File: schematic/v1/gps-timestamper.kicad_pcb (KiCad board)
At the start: 2 copper layers, 80 x 40 mm, 77 parts, among them J1 GPS, J2 Input, J3 PPS_OUT, J4 USB_OTG, J5 SWD, U1 MCP633, U2 MCP633, U3 APU1206K-33, U4 MCP633, U5 MCP633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

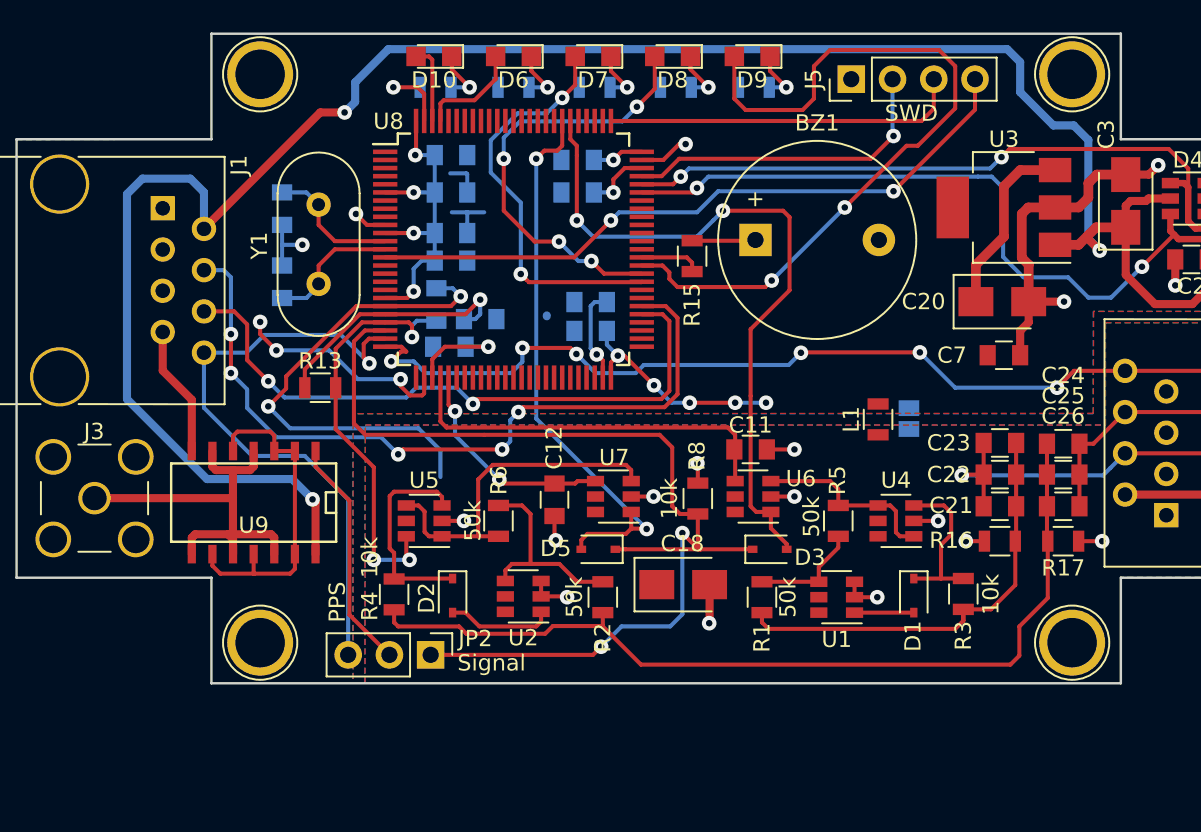
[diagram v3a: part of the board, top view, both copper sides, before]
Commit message: Fix for PCBs: op amps
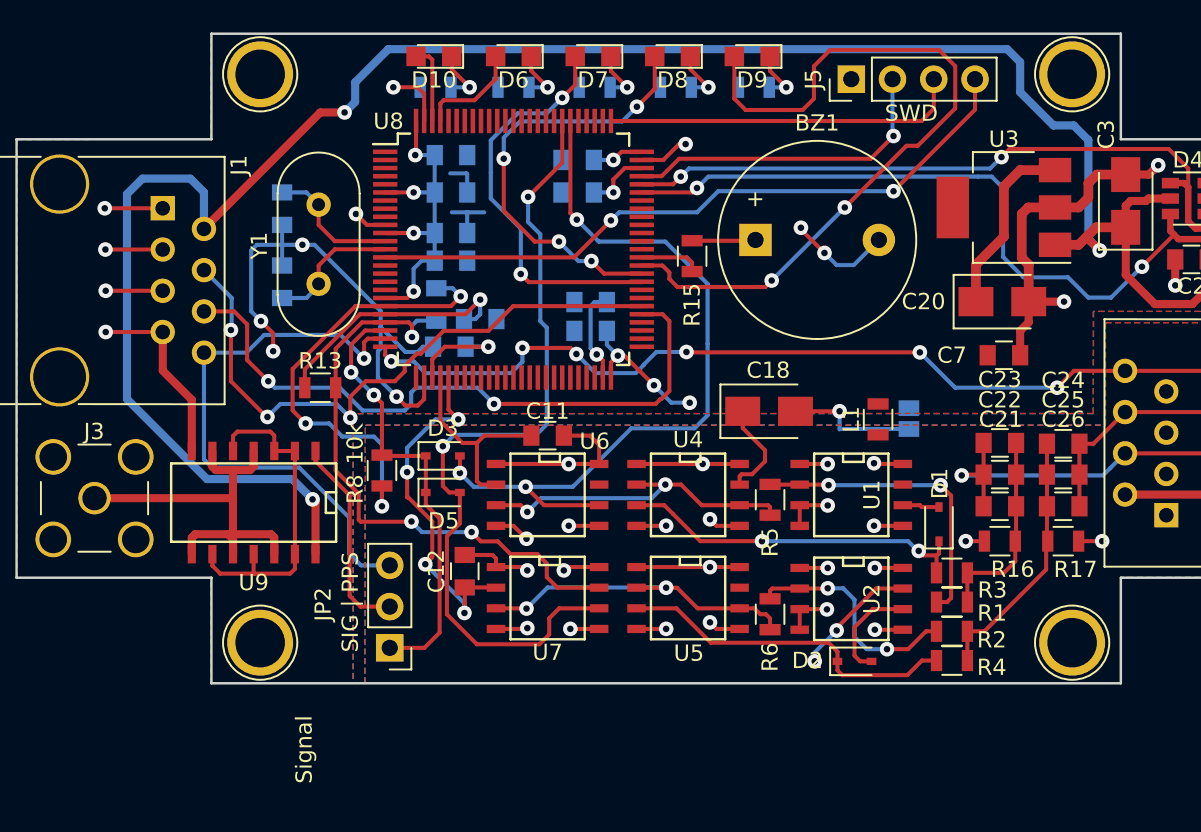
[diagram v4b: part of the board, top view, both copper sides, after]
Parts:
- U1, U2, U4, U5, U6, U7: footprint TO_SOT_Packages_SMD:SOT-23-6 -> SMD_Packages:SOIC-8-N
- U3: value APU1206K-33 -> MCP1826S
- moved R4 34.6 mm to (80.6, 61.6), turned to 0 degrees
- moved D2 25.1 mm to (74.6, 61.6), turned to 0 degrees
- moved R2 21.6 mm to (80.6, 59.8), turned to 0 degrees
- moved D3 20.9 mm to (49.2, 49.0)
- moved U2 20.2 mm to (74.4, 57.8), turned to 270 degrees
- moved R8 19.5 mm to (45.5, 49.9), turned to 90 degrees
- moved R6 17.7 mm to (69.4, 58.8)
- moved U5 16.9 mm to (64.3, 57.8), turned to 270 degrees
- moved U4 12.9 mm to (64.3, 51.4), turned to 270 degrees
- moved U6 12.7 mm to (55.7, 51.4), turned to 270 degrees
- moved C11 12.5 mm to (55.7, 47.8)
- moved C18 11.9 mm to (69.3, 46.2)
- moved R1 11.7 mm to (80.6, 58.0), turned to 0 degrees
- moved D5 10.2 mm to (49.2, 51.2), turned to 0 degrees
- moved U7 7.45 mm to (55.7, 57.8), turned to 270 degrees
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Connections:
- U1 pad 1: Net-(D1-Pad2) -> GNDA
- U1 pad 2: GNDA -> Net-(R1-Pad1)
- U1 pad 4: Net-(R1-Pad1) -> GNDA
- U1 pad 5: Net-(U1-Pad5) -> GNDA
- U1 pad 6: +3.3VA -> Net-(D1-Pad2)
- U2 pad 1: Net-(D2-Pad2) -> GNDA
- U2 pad 2: GNDA -> Net-(R2-Pad1)
- U2 pad 4: Net-(R2-Pad1) -> GNDA
- U2 pad 5: Net-(U2-Pad5) -> GNDA
- U2 pad 6: +3.3VA -> Net-(D2-Pad2)
- U4 pad 1: Net-(R5-Pad1) -> GNDA
- U4 pad 2: GNDA -> Net-(R5-Pad1)
- U4 pad 4: Net-(R5-Pad1) -> GNDA
- U4 pad 5: Net-(U4-Pad5) -> GNDA
- U4 pad 6: +3.3VA -> Net-(R5-Pad1)
- U5 pad 1: Net-(R6-Pad1) -> GNDA
- U5 pad 2: GNDA -> Net-(R6-Pad1)
- U5 pad 4: Net-(R6-Pad1) -> GNDA
- U5 pad 5: Net-(U5-Pad5) -> GNDA
- U5 pad 6: +3.3VA -> Net-(R6-Pad1)
- U6 pad 1: Net-(D3-Pad2) -> GNDA
- U6 pad 2: GNDA -> DAC_CH03
- U6 pad 4: DAC_CH03 -> GNDA
- U6 pad 5: Net-(U6-Pad5) -> GNDA
- U6 pad 6: +3.3VA -> Net-(D3-Pad2)
- U7 pad 1: Net-(D5-Pad2) -> GNDA
- U7 pad 2: GNDA -> DAC_CH47
- U7 pad 4: DAC_CH47 -> GNDA
- U7 pad 5: Net-(U7-Pad5) -> GNDA
- U7 pad 6: +3.3VA -> Net-(D5-Pad2)
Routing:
- net GNDA: track 50.2 -> 100.4 mm, vias 14 -> 27
- net Ch1_to_amp: track 55.6 -> 16.0 mm
- net TTL_IN: track 66.6 -> 27.5 mm
- net GND: track 68.0 -> 103.9 mm, vias 11 -> 17
- net +3.3VA: track 27.5 -> 51.8 mm, vias 4 -> 6
- net Net-(D5-Pad2): track 35.0 -> 50.1 mm
- net Ch0_to_amp: track 27.2 -> 12.4 mm
- net Net-(D1-Pad1): track 9.85 -> 21.8 mm, vias 0 -> 2
- net Net-(R1-Pad1): track 6.80 -> 18.7 mm, vias 0 -> 2
- net DAC_CH03: track 24.0 -> 12.6 mm
- net GPS_MCU_RX: track 47.5 -> 38.4 mm, vias 5 -> 3
- net Net-(R5-Pad1): track 11.6 -> 20.6 mm, vias 0 -> 2
- net DAC_CH47: track 13.7 -> 22.2 mm, vias 2 -> 4
- net Net-(D2-Pad1): track 12.8 -> 21.2 mm
- net +3V3: track 55.2 -> 50.5 mm, vias 11 -> 9
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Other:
- board text added: "SIG | PPS"
- board text removed: "PPS"

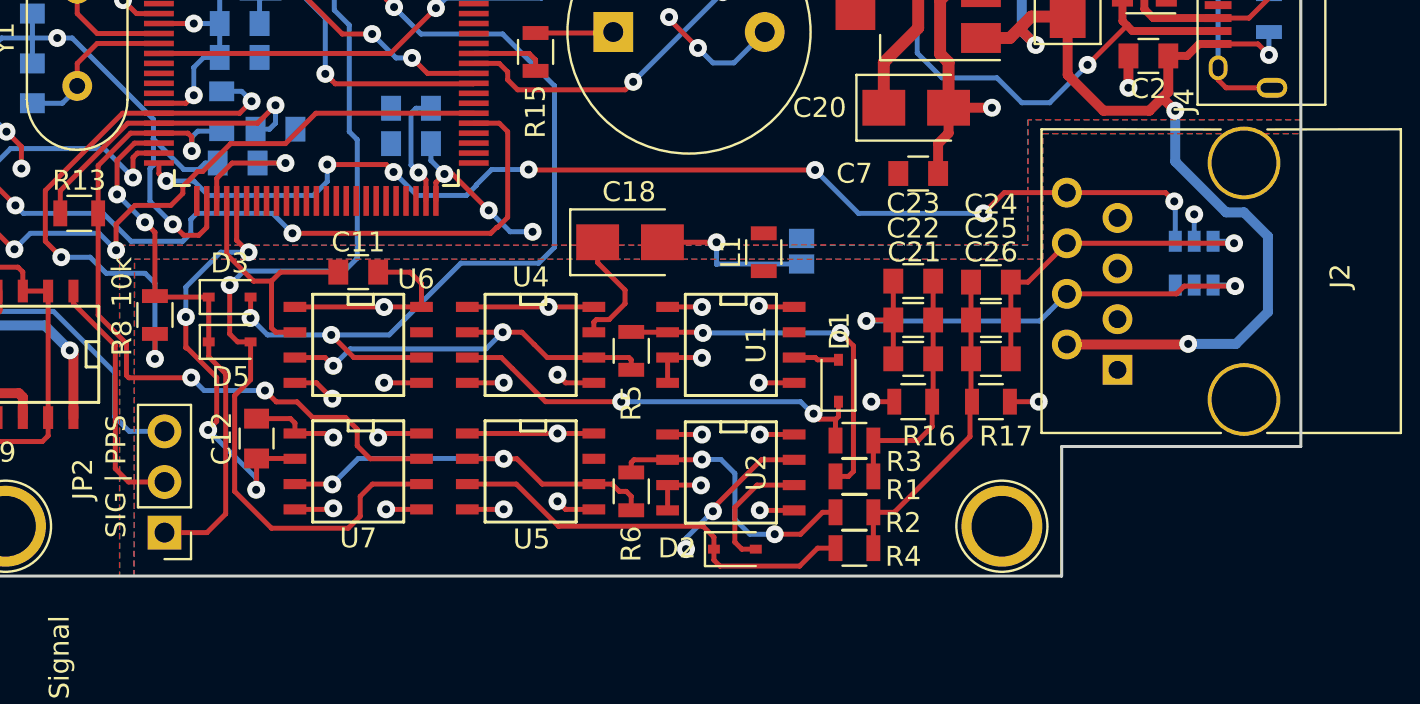
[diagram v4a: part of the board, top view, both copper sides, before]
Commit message: New fixed schematics
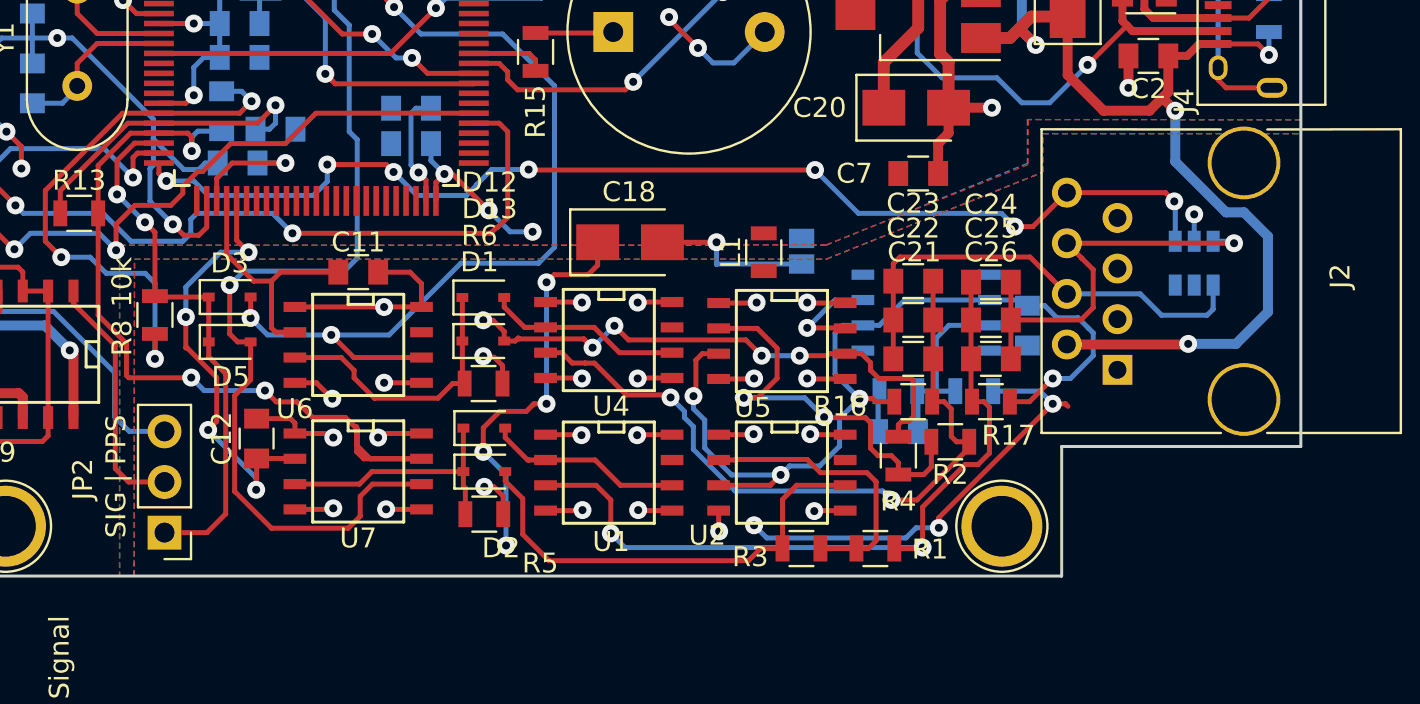
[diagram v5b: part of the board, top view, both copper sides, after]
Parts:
- added C27: 100n, Capacitors_SMD:C_0805, B.Cu at (82.8, 55.8)
- added C28: 100n, Capacitors_SMD:C_0805, B.Cu at (89.3, 50.4)
- added D12: 1N4148, Diodes_SMD:D_SOD-323, F.Cu at (62.0, 49.0)
- added D13: 1N4148, Diodes_SMD:D_SOD-323, F.Cu at (62.0, 51.2)
- added R18: 10k, Resistors_SMD:R_0805, B.Cu at (86.6, 53.7)
- added R19: 10k, Resistors_SMD:R_0805, B.Cu at (82.8, 53.7)
- added U10: MCP633, SMD_Packages:SOIC-8-N, B.Cu at (84.2, 49.8)
- R2: value 50k -> 47k
- R3: value 10k -> 50k
- R4: value 10k -> 47k
- R5, R6: value 50k -> 10k
- moved D1 17.9 mm to (62.0, 55.6), turned to 0 degrees
- moved U5 14.2 mm to (77.0, 51.2)
- moved D2 13.2 mm to (62.0, 57.8)
- moved R5 11.0 mm to (62.0, 59.9), turned to 0 degrees
- moved R6 9.17 mm to (62.0, 53.3), turned to 0 degrees
- moved U1 8.87 mm to (68.3, 57.8)
- moved R3 6.04 mm to (77.9, 61.6)
- moved R2 5.97 mm to (85.4, 56.3), turned to 180 degrees
- moved R4 5.14 mm to (82.8, 57.0), turned to 270 degrees
- moved U4 3.93 mm to (68.3, 51.2)
- moved R1 3.77 mm to (81.7, 61.6), turned to 180 degrees
- moved U2 2.56 mm to (77.0, 57.8)
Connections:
- D2 pad 1: Net-(D2-Pad1) -> Net-(D1-Pad1)
- R1 pad 1: Net-(R1-Pad1) -> Ch1_to_amp
- R1 pad 2: Ch0_to_amp -> Net-(R1-Pad2)
- R16 pad 2: GNDA -> GNDS
- R17 pad 1: GNDA -> GNDS
- R2 pad 1: Net-(R2-Pad1) -> Ch0_to_amp
- R2 pad 2: Ch1_to_amp -> Net-(R2-Pad2)
- R3 pad 1: Net-(D1-Pad1) -> Net-(D2-Pad2)
- R3 pad 2: Ch0_to_amp -> Net-(R1-Pad2)
- R4 pad 1: Net-(D2-Pad1) -> Net-(D13-Pad2)
- R4 pad 2: Ch1_to_amp -> Net-(R2-Pad2)
- R5 pad 1: Net-(R5-Pad1) -> Net-(D1-Pad1)
- R5 pad 2: Net-(R1-Pad1) -> GNDA
- R6 pad 1: Net-(R6-Pad1) -> Net-(D12-Pad1)
- R6 pad 2: Net-(R2-Pad1) -> GNDA
- U1 pad 2: Net-(R1-Pad1) -> Net-(D1-Pad2)
- U1 pad 3: GNDA -> Ch1_to_amp
- U2 pad 2: Net-(R2-Pad1) -> Net-(R1-Pad2)
- U2 pad 3: GNDA -> GNDS
- U4 pad 2: Net-(R5-Pad1) -> Net-(D12-Pad2)
- U4 pad 3: Net-(D1-Pad1) -> Ch0_to_amp
- U4 pad 6: Net-(R5-Pad1) -> Net-(D12-Pad2)
- U5 pad 2: Net-(R6-Pad1) -> Net-(R2-Pad2)
- U5 pad 3: Net-(D2-Pad1) -> GNDS
- U5 pad 6: Net-(R6-Pad1) -> Net-(D13-Pad2)
- U6 pad 3: Net-(R5-Pad1) -> Net-(D12-Pad1)
- U7 pad 3: Net-(R6-Pad1) -> Net-(D1-Pad1)
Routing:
- net GNDS: track 0.00 -> 46.2 mm, vias 0 -> 4
- net +3.3VA: track 51.8 -> 90.6 mm, vias 6 -> 12
- net Net-(D13-Pad2): track 0.00 -> 27.8 mm, vias 0 -> 5
- net Ch0_to_amp: track 12.4 -> 36.5 mm, vias 0 -> 2
- net Ch1_to_amp: track 16.0 -> 38.5 mm, vias 0 -> 2
- net Net-(D2-Pad1): track 21.2 -> 0.00 mm
- net Net-(R6-Pad1): track 20.7 -> 0.00 mm, vias 2 -> 0
- net Net-(R5-Pad1): track 20.6 -> 0.00 mm, vias 2 -> 0
- net Net-(R2-Pad2): track 0.00 -> 20.5 mm, vias 0 -> 2
- net Net-(R1-Pad1): track 18.7 -> 0.00 mm, vias 2 -> 0
- net Net-(D2-Pad2): track 6.38 -> 23.3 mm
- net Net-(R1-Pad2): track 0.00 -> 14.3 mm
- net Net-(D12-Pad1): track 0.00 -> 14.3 mm
- net Net-(R2-Pad1): track 14.2 -> 0.00 mm, vias 2 -> 0
- net Net-(D12-Pad2): track 0.00 -> 9.85 mm
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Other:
- rule pad_to_mask_clearance: 0.2 -> 0
- board text added: "GPS"
- board text added: "NRST SWCLK SWDIO GND"
- board text added: "OpenLDS lightning detector main board, v1.2"
- board text added: "PC"
- board text added: "SIGNAL"
- board text added: "SYNC OUT"
